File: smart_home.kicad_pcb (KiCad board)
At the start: 2 copper layers, 100 x 80 mm, 0 parts

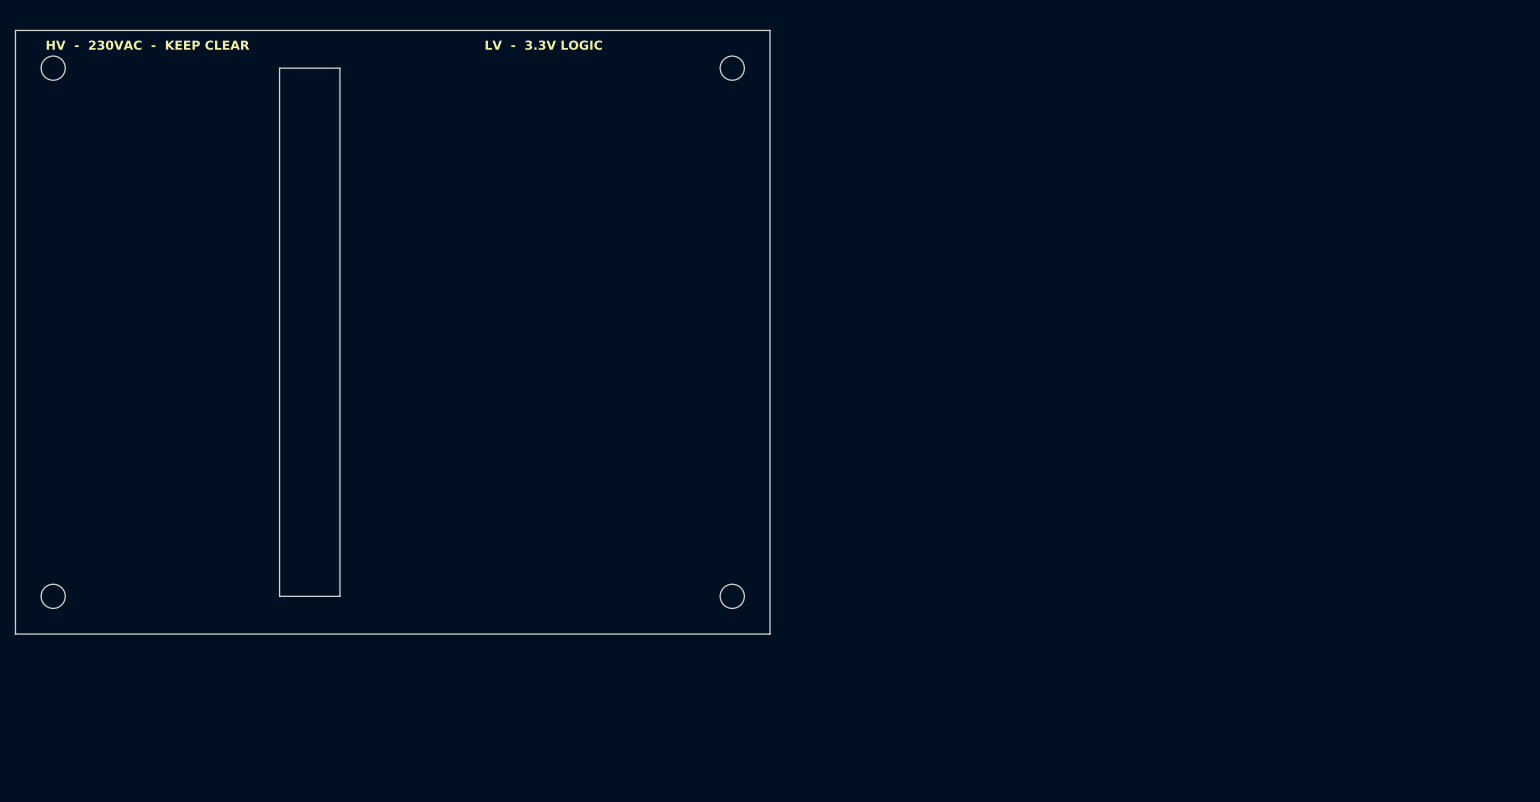
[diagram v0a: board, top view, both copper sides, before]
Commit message: Complete 4-channel smart home AC relay PCB design
Full KiCad 9 design for a 230V AC 4-channel smart home relay controller:
- ESP32-WROOM-32E + ULN2003A + 4x SANYOU SRD relays
- 4 isolated AC inputs (own L/N/PE + fuse per channel)
- 4 AC outputs (L_switched + N_passthrough per channel)
- HLK-PM01 isolated AC-DC + AMS1117-3.3 LDO for logic
- Per-channel current sense (4x ACS712-05B + ADC dividers)
- Per-channel voltage sense (ADS1115 I2C ADC + external ZMPT101B headers)
- 4-pin I2C header for 16x2 LCD module (PCF8574 backpack)
- Manual override buttons + status LEDs per channel
- 6-pin UART programming header
- Custom DRC: 4mm HV-LV clearance, 3mm HV-HV, 2mm HV trace minimum
- Physical HV/LV isolation slot in PCB

Layout: 200x100mm 2-layer FR4, 76 components, mostly routed (Freerouting).
21 HV channel-internal traces still need manual routing in KiCad.

Includes generator scripts (generate_sch.py, generate_pcb.py, add_acs712.py,
add_voltage_sense.py) that build everything from bom.csv. Fabrication
gerbers + drill + pick-and-place files in fabrication/.
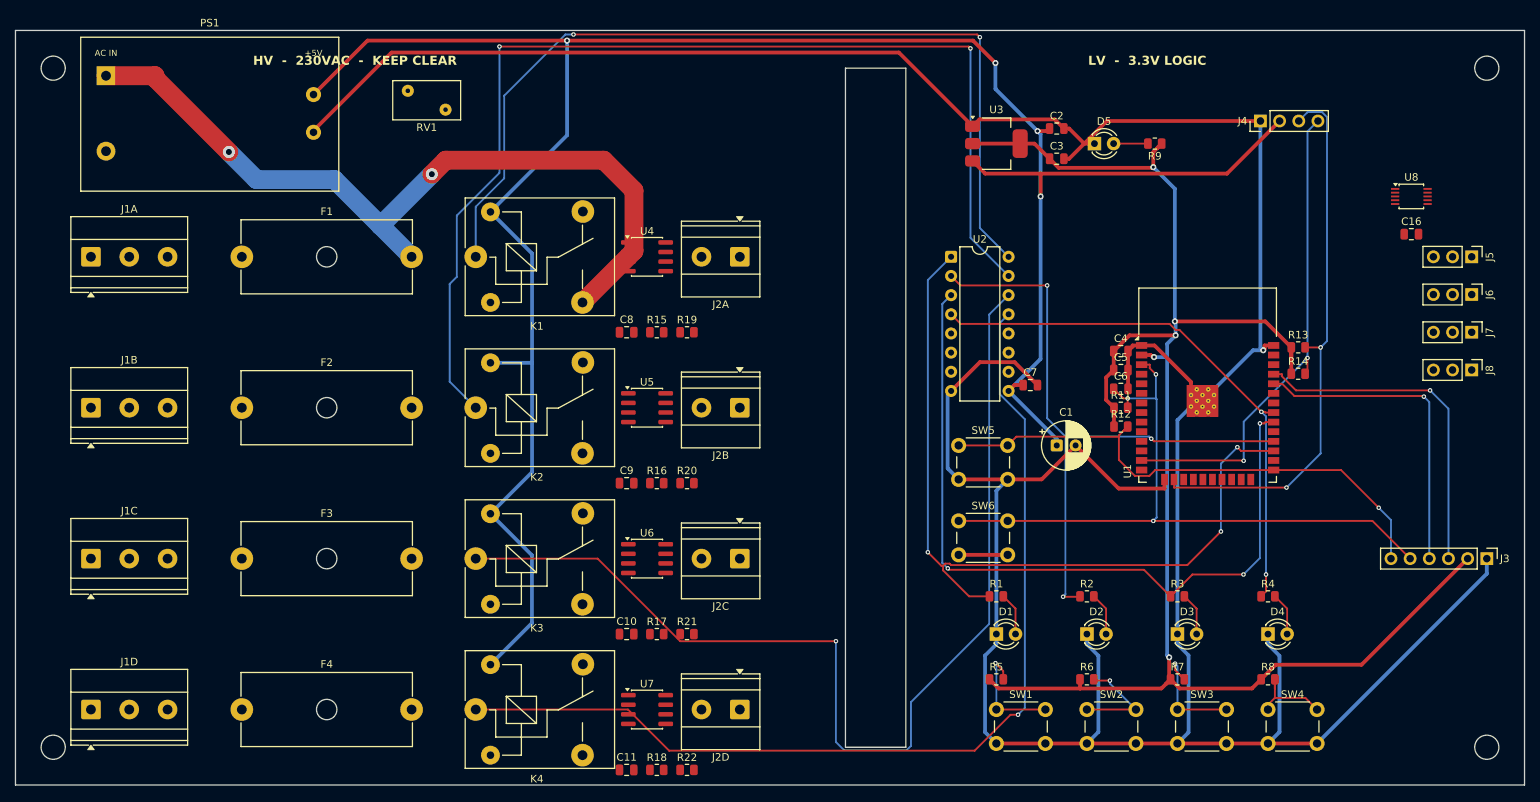
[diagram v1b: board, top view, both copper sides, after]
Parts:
- added C1: 100uF/16V, Capacitor_THT:CP_Radial_D6.3mm_P2.50mm, F.Cu at (138.0, 55.0)
- added C10: 100nF, Capacitor_SMD:C_0805_2012Metric, F.Cu at (81.0, 80.0)
- added C11: 100nF, Capacitor_SMD:C_0805_2012Metric, F.Cu at (81.0, 98.0)
- added C16: 100nF, Capacitor_SMD:C_0805_2012Metric, F.Cu at (185.0, 27.0)
- added C2: 10uF, Capacitor_SMD:C_0805_2012Metric, F.Cu at (138.0, 13.0)
- added C3: 22uF, Capacitor_SMD:C_0805_2012Metric, F.Cu at (138.0, 17.0)
- added C4: 10uF, Capacitor_SMD:C_0805_2012Metric, F.Cu at (146.5, 42.5)
- added C5: 100nF, Capacitor_SMD:C_0805_2012Metric, F.Cu at (146.5, 45.0)
- added C6: 1uF, Capacitor_SMD:C_0805_2012Metric, F.Cu at (146.5, 47.5)
- added C7: 100nF, Capacitor_SMD:C_0805_2012Metric, F.Cu at (134.5, 47.0)
- added C8: 100nF, Capacitor_SMD:C_0805_2012Metric, F.Cu at (81.0, 40.0)
- added C9: 100nF, Capacitor_SMD:C_0805_2012Metric, F.Cu at (81.0, 60.0)
- added D1: LED_Green, LED_THT:LED_D3.0mm, F.Cu at (130.0, 80.0)
- added D2: LED_Green, LED_THT:LED_D3.0mm, F.Cu at (142.0, 80.0)
- added D3: LED_Green, LED_THT:LED_D3.0mm, F.Cu at (154.0, 80.0)
- added D4: LED_Green, LED_THT:LED_D3.0mm, F.Cu at (166.0, 80.0)
- added D5: LED_Red, LED_THT:LED_D3.0mm, F.Cu at (143.0, 15.0)
- added F1: T4A, Fuse:Fuseholder_Cylinder-5x20mm_Schurter_0031_8201_Horizontal_Open, F.Cu at (30.0, 30.0)
- added F2: T4A, Fuse:Fuseholder_Cylinder-5x20mm_Schurter_0031_8201_Horizontal_Open, F.Cu at (30.0, 50.0)
- added F3: T4A, Fuse:Fuseholder_Cylinder-5x20mm_Schurter_0031_8201_Horizontal_Open, F.Cu at (30.0, 70.0)
- added F4: T4A, Fuse:Fuseholder_Cylinder-5x20mm_Schurter_0031_8201_Horizontal_Open, F.Cu at (30.0, 90.0)
- added J1A: AC_IN_1, TerminalBlock_Phoenix:TerminalBlock_Phoenix_MKDS-1,5-3-5.08_1x03_P5.08mm_Horizontal, F.Cu at (10.0, 30.0)
- added J1B: AC_IN_2, TerminalBlock_Phoenix:TerminalBlock_Phoenix_MKDS-1,5-3-5.08_1x03_P5.08mm_Horizontal, F.Cu at (10.0, 50.0)
- added J1C: AC_IN_3, TerminalBlock_Phoenix:TerminalBlock_Phoenix_MKDS-1,5-3-5.08_1x03_P5.08mm_Horizontal, F.Cu at (10.0, 70.0)
- added J1D: AC_IN_4, TerminalBlock_Phoenix:TerminalBlock_Phoenix_MKDS-1,5-3-5.08_1x03_P5.08mm_Horizontal, F.Cu at (10.0, 90.0)
- added J2A: LOAD_1, TerminalBlock_Phoenix:TerminalBlock_Phoenix_MKDS-1,5-2-5.08_1x02_P5.08mm_Horizontal, F.Cu at (96.0, 30.0)
- added J2B: LOAD_2, TerminalBlock_Phoenix:TerminalBlock_Phoenix_MKDS-1,5-2-5.08_1x02_P5.08mm_Horizontal, F.Cu at (96.0, 50.0)
- added J2C: LOAD_3, TerminalBlock_Phoenix:TerminalBlock_Phoenix_MKDS-1,5-2-5.08_1x02_P5.08mm_Horizontal, F.Cu at (96.0, 70.0)
- added J2D: LOAD_4, TerminalBlock_Phoenix:TerminalBlock_Phoenix_MKDS-1,5-2-5.08_1x02_P5.08mm_Horizontal, F.Cu at (96.0, 90.0)
- added J3: PROG, Connector_PinHeader_2.54mm:PinHeader_1x06_P2.54mm_Vertical, F.Cu at (195.0, 70.0)
- added J4: LCD I2C, Connector_PinHeader_2.54mm:PinHeader_1x04_P2.54mm_Vertical, F.Cu at (165.0, 12.0)
- added J5: V_SENSE_1, Connector_PinHeader_2.54mm:PinHeader_1x03_P2.54mm_Vertical, F.Cu at (193.0, 30.0)
- added J6: V_SENSE_2, Connector_PinHeader_2.54mm:PinHeader_1x03_P2.54mm_Vertical, F.Cu at (193.0, 35.0)
- added J7: V_SENSE_3, Connector_PinHeader_2.54mm:PinHeader_1x03_P2.54mm_Vertical, F.Cu at (193.0, 40.0)
- added J8: V_SENSE_4, Connector_PinHeader_2.54mm:PinHeader_1x03_P2.54mm_Vertical, F.Cu at (193.0, 45.0)
- added K1: SRD-05VDC-SL-C, Relay_THT:Relay_SPDT_SANYOU_SRD_Series_Form_C, F.Cu at (61.0, 30.0)
- added K2: SRD-05VDC-SL-C, Relay_THT:Relay_SPDT_SANYOU_SRD_Series_Form_C, F.Cu at (61.0, 50.0)
- added K3: SRD-05VDC-SL-C, Relay_THT:Relay_SPDT_SANYOU_SRD_Series_Form_C, F.Cu at (61.0, 70.0)
- added K4: SRD-05VDC-SL-C, Relay_THT:Relay_SPDT_SANYOU_SRD_Series_Form_C, F.Cu at (61.0, 90.0)
- added PS1: HLK-PM01, hlk_pm01:HLK-PM01, F.Cu at (12.0, 6.00)
- added R1: 1k, Resistor_SMD:R_0805_2012Metric, F.Cu at (130.0, 75.0)
- added R11: 10k, Resistor_SMD:R_0805_2012Metric, F.Cu at (146.5, 50.0)
- added R12: 10k, Resistor_SMD:R_0805_2012Metric, F.Cu at (146.5, 52.5)
- added R13: 4.7k, Resistor_SMD:R_0805_2012Metric, F.Cu at (170.0, 42.0)
- added R14: 4.7k, Resistor_SMD:R_0805_2012Metric, F.Cu at (170.0, 45.5)
- added R15: 10k, Resistor_SMD:R_0805_2012Metric, F.Cu at (85.0, 40.0)
- added R16: 10k, Resistor_SMD:R_0805_2012Metric, F.Cu at (85.0, 60.0)
- added R17: 10k, Resistor_SMD:R_0805_2012Metric, F.Cu at (85.0, 80.0)
- added R18: 10k, Resistor_SMD:R_0805_2012Metric, F.Cu at (85.0, 98.0)
- added R19: 18k, Resistor_SMD:R_0805_2012Metric, F.Cu at (89.0, 40.0)
- added R2: 1k, Resistor_SMD:R_0805_2012Metric, F.Cu at (142.0, 75.0)
- added R20: 18k, Resistor_SMD:R_0805_2012Metric, F.Cu at (89.0, 60.0)
- added R21: 18k, Resistor_SMD:R_0805_2012Metric, F.Cu at (89.0, 80.0)
- added R22: 18k, Resistor_SMD:R_0805_2012Metric, F.Cu at (89.0, 98.0)
- added R3: 1k, Resistor_SMD:R_0805_2012Metric, F.Cu at (154.0, 75.0)
- added R4: 1k, Resistor_SMD:R_0805_2012Metric, F.Cu at (166.0, 75.0)
- added R5: 10k, Resistor_SMD:R_0805_2012Metric, F.Cu at (130.0, 86.0)
- added R6: 10k, Resistor_SMD:R_0805_2012Metric, F.Cu at (142.0, 86.0)
- added R7: 10k, Resistor_SMD:R_0805_2012Metric, F.Cu at (154.0, 86.0)
- added R8: 10k, Resistor_SMD:R_0805_2012Metric, F.Cu at (166.0, 86.0)
- added R9: 1k, Resistor_SMD:R_0805_2012Metric, F.Cu at (151.0, 15.0)
- added RV1: S07K275, Varistor:RV_Disc_D9mm_W5.2mm_P5mm, F.Cu at (52.0, 8.00)
- added SW1: TACT_6mm, Button_Switch_THT:SW_PUSH_6mm, F.Cu at (130.0, 90.0)
- added SW2: TACT_6mm, Button_Switch_THT:SW_PUSH_6mm, F.Cu at (142.0, 90.0)
- added SW3: TACT_6mm, Button_Switch_THT:SW_PUSH_6mm, F.Cu at (154.0, 90.0)
- added SW4: TACT_6mm, Button_Switch_THT:SW_PUSH_6mm, F.Cu at (166.0, 90.0)
- added SW5: TACT_6mm, Button_Switch_THT:SW_PUSH_6mm, F.Cu at (125.0, 55.0)
- added SW6: TACT_6mm, Button_Switch_THT:SW_PUSH_6mm, F.Cu at (125.0, 65.0)
- added U1: ESP32-WROOM-32E, RF_Module:ESP32-WROOM-32, F.Cu at (158.0, 50.0)
- added U2: ULN2003A, Package_DIP:DIP-16_W7.62mm, F.Cu at (124.0, 30.0)
- added U3: AMS1117-3.3, Package_TO_SOT_SMD:SOT-223-3_TabPin2, F.Cu at (130.0, 15.0)
- added U4: ACS712-05B, Package_SO:SOIC-8_3.9x4.9mm_P1.27mm, F.Cu at (83.7, 30.0)
- added U5: ACS712-05B, Package_SO:SOIC-8_3.9x4.9mm_P1.27mm, F.Cu at (83.7, 50.0)
- added U6: ACS712-05B, Package_SO:SOIC-8_3.9x4.9mm_P1.27mm, F.Cu at (83.7, 70.0)
- added U7: ACS712-05B, Package_SO:SOIC-8_3.9x4.9mm_P1.27mm, F.Cu at (83.7, 90.0)
- added U8: ADS1115, Package_SO:TSSOP-10_3x3mm_P0.5mm, F.Cu at (185.0, 22.0)
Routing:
- net GND: track 0.00 -> 479.9 mm, vias 0 -> 1
- net +5V: track 0.00 -> 305.0 mm, vias 0 -> 4
- net +3V3: track 0.00 -> 218.8 mm, vias 0 -> 5
- net COIL2: track 0.00 -> 146.8 mm, vias 0 -> 2
- net COIL3: track 0.00 -> 141.4 mm, vias 0 -> 1
- net COIL4: track 0.00 -> 131.4 mm, vias 0 -> 1
- net COIL1: track 0.00 -> 120.2 mm, vias 0 -> 2
- net IO16: track 0.00 -> 107.3 mm, vias 0 -> 3
- net L1: track 0.00 -> 107.2 mm, vias 0 -> 2
- net IO18: track 0.00 -> 102.6 mm, vias 0 -> 3
- net EN: track 0.00 -> 91.6 mm, vias 0 -> 3
- net IO17: track 0.00 -> 85.8 mm, vias 0 -> 3
- net SDA_LCD: track 0.00 -> 73.9 mm, vias 0 -> 2
- net IO19: track 0.00 -> 73.1 mm, vias 0 -> 2
- net IO0: track 0.00 -> 72.6 mm, vias 0 -> 1
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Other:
- board size 100 x 80 mm -> 200 x 100 mm

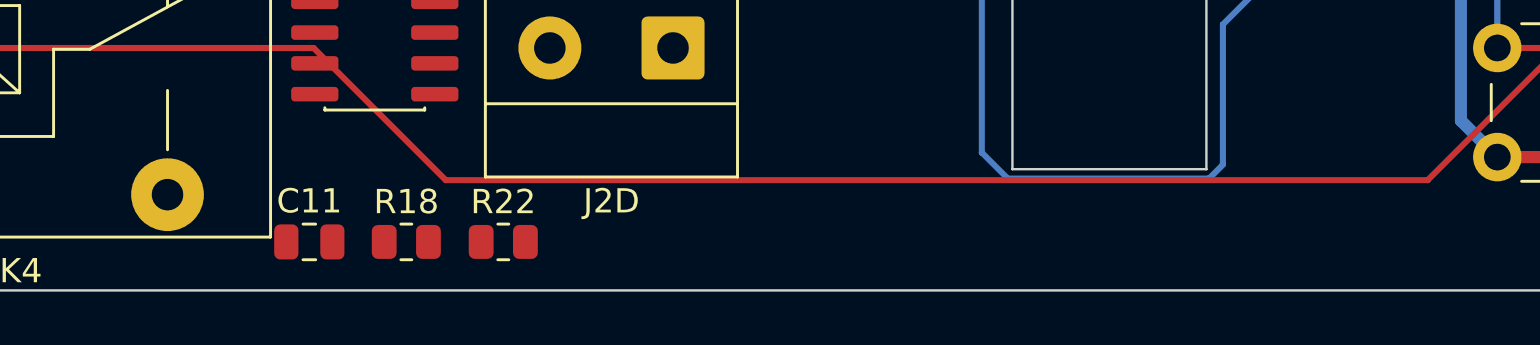
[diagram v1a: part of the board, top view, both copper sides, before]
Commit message: Add full component details to README and company name to PCB
- Update company in title block: Wisright -> WisRight Technologies Private Limited
  (smart_home.kicad_sch, smart_home.kicad_pcb, generate_sch.py)
- Add silkscreen on PCB:
  * Front silk (bottom center): "WisRight Technologies Private Limited" (bold 1.4mm)
  * Back silk (top, mirrored): "Smart Home 4-Channel AC Relay Controller - Rev 0.1"
  * Back silk (bottom, mirrored): "(c) 2026 WisRight Technologies Pvt Ltd"
- Expand README with detailed components list (active devices, passives,
  switches, connectors, external modules, custom lib parts)
- Add LICENSE file (MIT with WisRight copyright)
- Regenerate fabrication gerbers with updated silkscreen
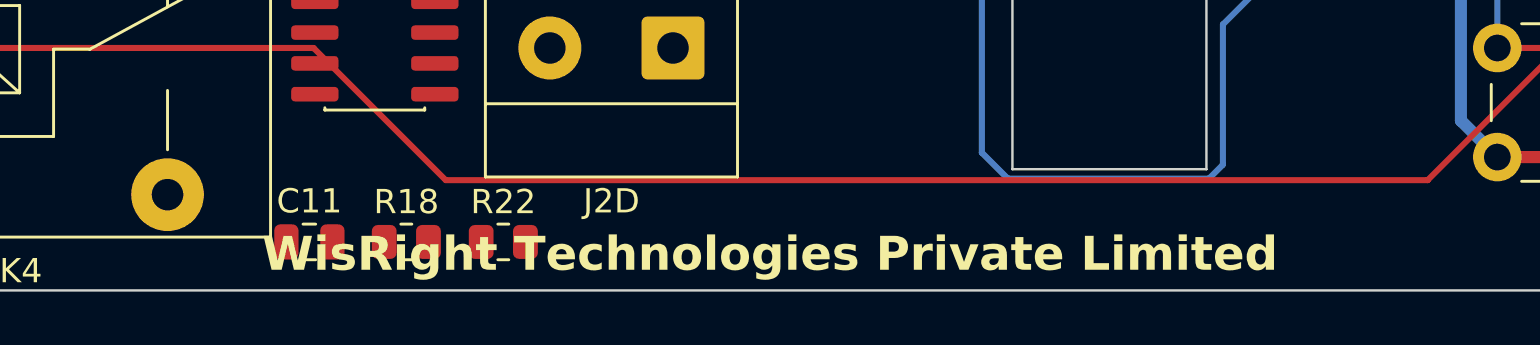
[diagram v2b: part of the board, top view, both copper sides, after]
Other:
- board text added: "(c) 2026 WisRight Technologies Pvt Ltd"
- board text added: "Smart Home 4-Channel AC Relay Controller - Rev 0.1"
- board text added: "WisRight Technologies Private Limited"
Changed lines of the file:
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@@
 		(date "2026-05-26")
 		(rev "0.1")
-		(company "Wisright")
+		(company "WisRight Technologies Private Limited")
 	)
 	(layers
@@
 		)
 	)
+	(gr_text "WisRight Technologies Private Limited"
+		(at 100 98.5 0)
+		(layer "F.SilkS")
+		(effects
+			(font
+				(size 1.4 1.4)
+				(thickness 0.22)
+				(bold yes)
+			)
+		)
+	)
+	(gr_text "Smart Home 4-Channel AC Relay Controller  -  Rev 0.1"
+		(at 100 2 0)
+		(layer "B.SilkS")
+		(effects
+			(font
+				(size 1.0 1.0)
+				(thickness 0.15)
+			)
+			(justify mirror)
+		)
+	)
+	(gr_text "(c) 2026 WisRight Technologies Pvt Ltd"
+		(at 100 98 0)
+		(layer "B.SilkS")
+		(effects
+			(font
+				(size 1.0 1.0)
+				(thickness 0.15)
+			)
+			(justify mirror)
+		)
+	)
